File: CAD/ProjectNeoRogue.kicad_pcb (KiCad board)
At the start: 4 copper layers, 95.5 x 113.7 mm, 85 parts, among them J1 5v GND, J2 Micro_SD_Card, J3 JTAG, J4 UART, J5 Reset Jumper, J6 Boot Jumper, J7 RoundDisplay_SPI, J8 USB_C_Plug_USB2.0, J9 RoundDisplay_SPI_v2, SW1 SW_SPDT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

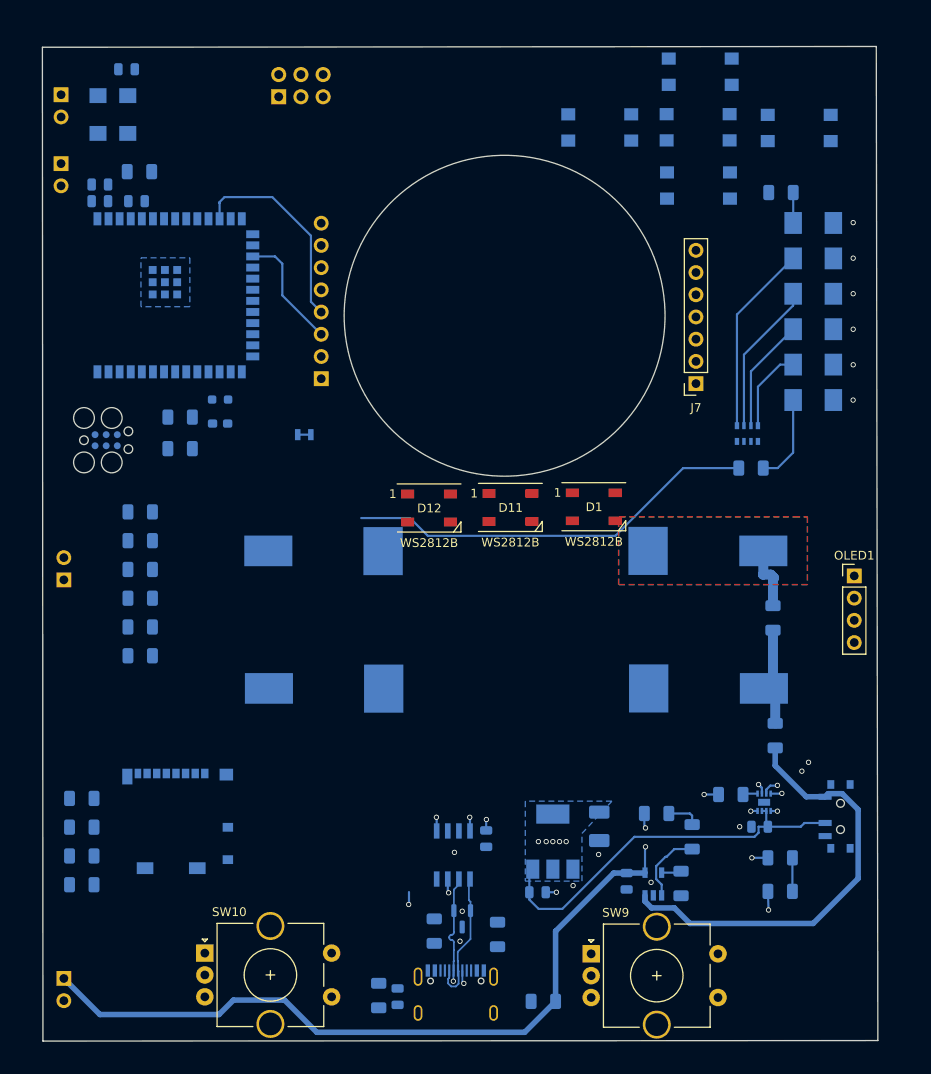
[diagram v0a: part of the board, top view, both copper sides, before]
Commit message: routing and removing buttons OLED
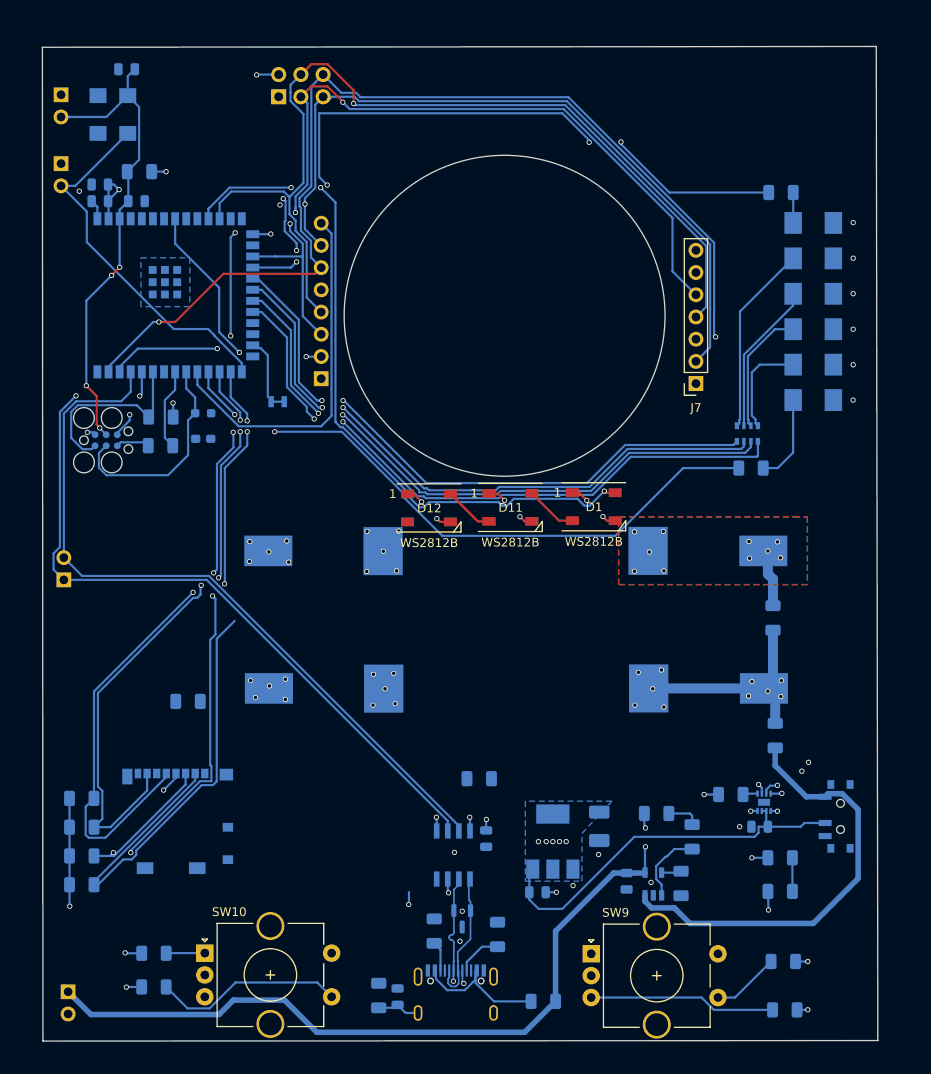
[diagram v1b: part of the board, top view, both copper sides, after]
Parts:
- removed OLED1: OLED, Connector_PinHeader_2.54mm:PinHeader_1x04_P2.54mm_Vertical
- removed SW4: SW_Up, BadgePirates:SW_SPST_TL3305C(small)
- removed SW5: SW_Center, BadgePirates:SW_SPST_TL3305C(small)
- removed SW6: SW_Right, BadgePirates:SW_SPST_TL3305C(small)
- removed SW7: SW_Down, BadgePirates:SW_SPST_TL3305C(small)
- removed SW8: SW_Left, BadgePirates:SW_SPST_TL3305C(small)
- moved R15 91.2 mm to (207.7, 155.9), turned to 0 degrees
- moved R16 86.1 mm to (207.5, 150.4), turned to 180 degrees
- moved R14 49.3 mm to (172.8, 129.5)
- moved R17 40.6 mm to (135.6, 149.5)
- moved R19 37.9 mm to (135.6, 153.3)
- moved R18 10.1 mm to (139.5, 120.7)
- moved JP1 4.84 mm to (150.0, 86.4)
- moved C11 2.60 mm to (141.2, 90.6)
- moved R21 2.49 mm to (141.2, 87.7)
- moved R24 2.27 mm to (136.3, 91.4)
- moved R22 2.20 mm to (136.4, 88.1)
- moved J1 1.60 mm to (125.8, 153.9)
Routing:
- net IO02: track 0.00 -> 120.4 mm, vias 0 -> 5
- net IO01: track 0.00 -> 119.7 mm, vias 0 -> 2
- net USB_TX_ESP_RX: track 0.00 -> 89.2 mm, vias 0 -> 2
- net USB_RX_ESP_TX: track 0.00 -> 85.9 mm
- net IO10: track 0.00 -> 83.2 mm, vias 0 -> 6
- net IO08: track 103.3 -> 185.5 mm, vias 2 -> 3
- net IO09: track 98.9 -> 179.8 mm, vias 2 -> 5
- net IO18: track 0.00 -> 80.6 mm, vias 0 -> 3
- net IO35: track 0.00 -> 80.0 mm, vias 0 -> 6
- net IO36: track 0.00 -> 74.7 mm, vias 0 -> 4
- net IO14: track 0.00 -> 73.9 mm, vias 0 -> 2
- net IO13: track 0.00 -> 72.9 mm, vias 0 -> 2
- net IO12: track 0.00 -> 72.4 mm, vias 0 -> 2
- net IO11: track 0.00 -> 71.3 mm, vias 0 -> 2
- net IO37: track 0.00 -> 70.4 mm, vias 0 -> 4
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
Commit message: Update ProjectNeoRogue.kicad_pcb
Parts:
- moved R18 32.3 mm to (135.5, 152.8)
- moved R19 25.7 mm to (160.1, 145.9), turned to 180 degrees
- moved R17 3.09 mm to (135.5, 146.4)
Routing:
- net IO05: track 21.3 -> 186.4 mm, vias 0 -> 6
- net IO04: track 0.00 -> 142.9 mm, vias 0 -> 9
- net IO17: track 0.00 -> 107.2 mm, vias 0 -> 4
- net IO16: track 4.43 -> 102.2 mm, vias 0 -> 4
- net IO19: track 21.8 -> 10.2 mm
- net VCC: track 50.9 -> 57.1 mm, vias 25 -> 26
- net GND: track 20.2 -> 18.6 mm, vias 45 -> 48
- net IO02: track 120.4 -> 119.3 mm
- net IO10: track 83.2 -> 82.4 mm
- net IO14: track 73.9 -> 74.6 mm
- net IO08: track 185.5 -> 184.9 mm

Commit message: updates
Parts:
- added J10: Conn_01x01_Socket, Connector_PinHeader_2.54mm:PinHeader_1x01_P2.54mm_Vertical, B.Cu at (134.0, 98.0)
- J2: footprint Connector_Card:microSD_HC_Molex_104031-0811 -> BadgePirates:TF_PUSH
- moved R12 20.6 mm to (128.9, 117.8)
- moved R13 20.6 mm to (128.9, 121.1)
- moved R5 20.6 mm to (128.9, 111.2)
- moved R6 20.6 mm to (128.9, 114.5)
- moved J2 0.75 mm to (138.8, 133.9), turned to 90 degrees
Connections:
- J2 pad 10: (no net) -> GND
- J2 pad 2: IO34 -> unconnected-(J2-DAT3/CD-Pad2)
- J2 pad 3: IO35 -> IO34
- J2 pad 4: VCC -> IO35
- J2 pad 5: IO36 -> VCC
- J2 pad 6: GND -> IO36
- J2 pad 7: IO37 -> GND
- J2 pad 8: unconnected-(J2-DAT1-Pad8) -> IO37
- J2 pad 9: GND -> unconnected-(J2-DET-Pad9)
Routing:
- net IO34: track 55.9 -> 0.81 mm
- net IO35: track 80.0 -> 43.9 mm, vias 6 -> 4
- net IO36: track 74.7 -> 40.3 mm
- net IO37: track 70.4 -> 41.5 mm
- net IO04: track 142.9 -> 131.6 mm, vias 9 -> 7
- net VCC: track 57.1 -> 54.6 mm, vias 26 -> 25
- net GND: track 18.6 -> 20.5 mm, vias 48 -> 50
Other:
- board text removed: "MicroSD"

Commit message: routing and cleanup
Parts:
- moved J1 5.60 mm to (127.3, 148.5)
- moved R6 3.33 mm to (128.9, 111.2)
- moved R5 3.14 mm to (128.9, 114.4)
- moved J4 2.81 mm to (127.9, 105.9)
- moved J10 1.02 mm to (134.0, 97.0)
- moved J8 0.60 mm to (170.1, 152.7)
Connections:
- net SCL renamed IO07
- net SDA renamed IO06
- U2 pad 13: unconnected-(U2-GPIO19/U1RTS/ADC2_CH8/CLK_OUT2/USB_D--Pad13) -> IO19
- U2 pad 16: IO46 -> unconnected-(U2-GPIO46-Pad16)
- U2 pad 23: IO21 -> unconnected-(U2-GPIO21-Pad23)
- U2 pad 24: IO47 -> unconnected-(U2-GPIO47/SPICLK_P/SUBSPICLK_P_DIFF-Pad24)
- U2 pad 26: IO45 -> unconnected-(U2-GPIO45-Pad26)
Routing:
- net IO19: track 10.2 -> 98.2 mm, vias 0 -> 4
- net IO34: track 0.81 -> 48.0 mm, vias 0 -> 6
- net IO37: track 41.5 -> 73.9 mm
- net IO36: track 40.3 -> 71.7 mm
- net IO35: track 43.9 -> 69.2 mm
- net IO05: track 186.4 -> 167.2 mm, vias 6 -> 10
- net TDI: track 0.00 -> 16.2 mm, vias 0 -> 2
- net /Power/BATTERY2+: track 26.9 -> 13.7 mm
- net IO04: track 131.6 -> 142.8 mm
- net Boot: track 42.2 -> 48.0 mm
- net IO01: track 119.7 -> 124.3 mm
- net IO15: track 90.5 -> 94.3 mm
- net IO02: track 119.3 -> 123.1 mm
- net Net-(C11-Pad1): track 0.00 -> 2.94 mm
- net RESET: track 54.9 -> 57.6 mm
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- added copper zone on B.Cu, net /Power/BATTERY2+
- removed copper zone on F.Cu, net /Power/BATTERY1+

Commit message: Updated pins and moar
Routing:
- net Boot: track 48.0 -> 47.4 mm
- net GND: vias 52 -> 44
- net /Power/BATTERY2+: vias 10 -> 0
- net /Power/BATTERY1+: vias 10 -> 0

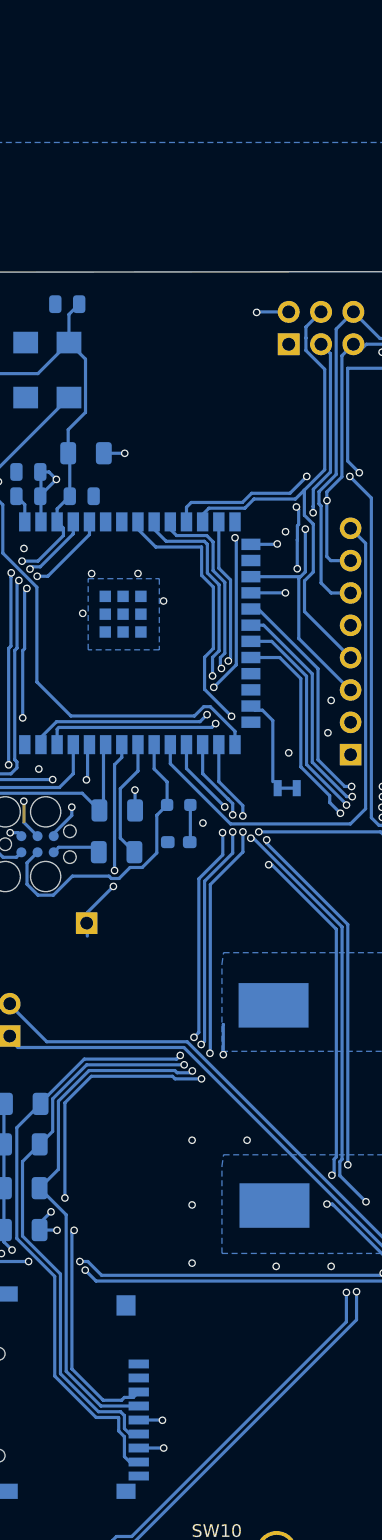
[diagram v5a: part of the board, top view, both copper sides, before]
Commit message: Updated layout
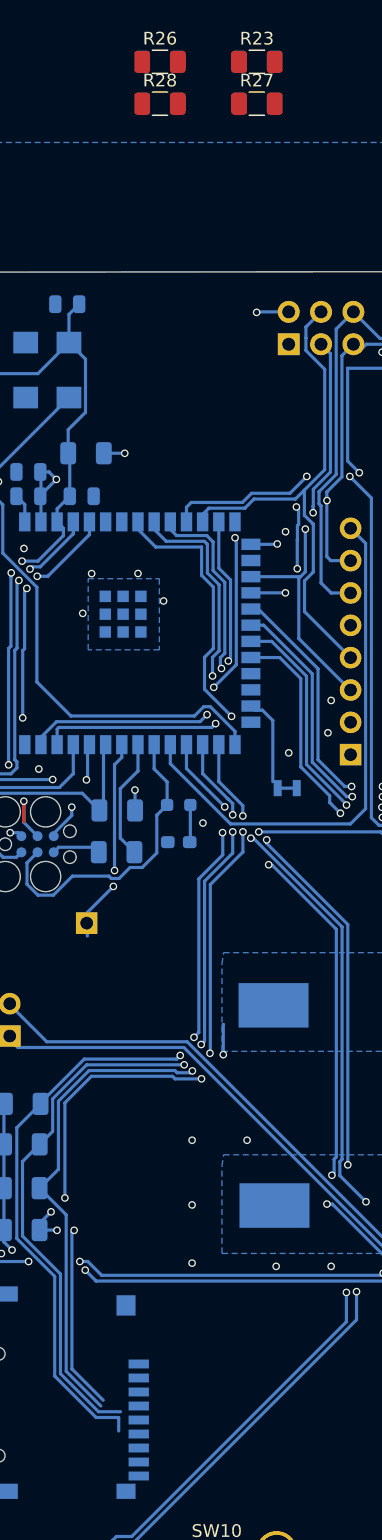
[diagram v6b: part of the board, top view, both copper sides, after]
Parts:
- added R23: 4.7k, BadgePirates:R_1206_3216Metric, F.Cu at (147.3, 29.3)
- added R26: 4.7k, BadgePirates:R_1206_3216Metric, F.Cu at (139.7, 29.3)
- added R27: 4.7k, BadgePirates:R_1206_3216Metric, F.Cu at (147.3, 32.6)
- added R28: 4.7k, BadgePirates:R_1206_3216Metric, F.Cu at (139.7, 32.6)
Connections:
- J2 pad 2: unconnected-(J2-DAT3/CD-Pad2) -> IO47
- J2 pad 3: IO34 -> IO35
- J2 pad 4: IO35 -> VCC
- J2 pad 5: VCC -> IO36
- J2 pad 6: IO36 -> GND
- J2 pad 7: GND -> IO37
- J2 pad 8: IO37 -> unconnected-(J2-DAT1-Pad8)
- R13 pad 1: IO34 -> IO47
- R16 pad 2: IO25 -> IO20
- SW9 pad S1: IO25 -> IO20
- U2 pad 14: unconnected-(U2-GPIO20/U1CTS/ADC2_CH9/CLK_OUT1/USB_D+-Pad14) -> IO20
- U2 pad 15: IO03 -> unconnected-(U2-GPIO3/TOUCH3/ADC1_CH2-Pad15)
- U2 pad 24: unconnected-(U2-GPIO47/SPICLK_P/SUBSPICLK_P_DIFF-Pad24) -> IO47
- U5 pad 7: IO09 -> IO07
- U5 pad 8: IO08 -> IO06
- X1 pad 3: IO08 -> IO06
- X1 pad 4: IO09 -> IO07
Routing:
- net IO34: track 48.0 -> 0.00 mm, vias 6 -> 0
- net IO47: track 0.00 -> 45.0 mm, vias 0 -> 6
- net IO25: track 7.78 -> 0.00 mm
- net IO20: track 0.00 -> 7.78 mm
- net IO37: track 73.9 -> 70.4 mm
- net IO35: track 69.2 -> 66.3 mm
- net IO36: track 71.7 -> 69.0 mm
- net unconnected-(U2-GPIO3/TOUCH3/ADC1_CH2-Pad15): track 0.00 -> 2.08 mm, vias 0 -> 1
- net IO03: track 2.08 -> 0.00 mm, vias 1 -> 0
- net GND: track 20.5 -> 18.6 mm, vias 44 -> 43
- net VCC: track 54.1 -> 52.3 mm, vias 25 -> 24

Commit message: Routing progress
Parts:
- added JP2: GPIO1, BadgePirates:SMT-JUMPER_2_NC_TRACE_NO-SILK, F.Cu at (-4.23, -0.13)
- added JP3: GPIO1, BadgePirates:SMT-JUMPER_2_NC_TRACE_NO-SILK, F.Cu at (-4.23, 2.14)
- added R29: 10k, BadgePirates:R_1206_3216Metric, F.Cu at (-8.36, 0.38)
- added R30: 10k, BadgePirates:R_1206_3216Metric, F.Cu at (-8.36, 3.67)
- D9: value Pwr -> PWR
- R21: value 75 -> 75k
- R23, R26, R27, R28: moved to B.Cu
- R24: value 22 -> 22k
- SW1: value SW_SPDT -> On/Off
- moved R26 121.8 mm to (214.9, 125.2), turned to -90 degrees
- moved R28 117.5 mm to (212.1, 125.2), turned to 90 degrees
- moved R23 70.7 mm to (202.4, 73.7), turned to 180 degrees
- moved R27 66.4 mm to (202.4, 69.6), turned to 180 degrees
- moved R4 0.12 mm to (133.9, 60.2)
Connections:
- J9 pad 5: IO33 -> IO21
- U2 pad 16: unconnected-(U2-GPIO46-Pad16) -> IO46
- U2 pad 23: unconnected-(U2-GPIO21-Pad23) -> IO21
- U2 pad 26: unconnected-(U2-GPIO45-Pad26) -> IO45
- X1 pad 5: IO01 -> Net-(JP2-B)
- X1 pad 6: IO02 -> Net-(JP3-A)
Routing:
- net IO20: track 7.78 -> 135.5 mm, vias 0 -> 4
- net IO09: track 178.4 -> 57.0 mm, vias 5 -> 2
- net IO08: track 184.7 -> 102.0 mm, vias 3 -> 4
- net IO10: track 80.3 -> 40.3 mm
- net IO47: track 45.0 -> 79.8 mm, vias 6 -> 8
- net IO02: track 123.1 -> 98.3 mm, vias 5 -> 7
- net GND: track 18.6 -> 23.0 mm, vias 43 -> 114
- net IO01: track 124.3 -> 128.2 mm, vias 2 -> 1
- net IO35: track 66.3 -> 68.8 mm
- net IO36: track 69.0 -> 70.7 mm
- net IO06: track 0.00 -> 1.68 mm
- net VCC: track 52.3 -> 53.9 mm, vias 24 -> 26
- net IO37: track 70.4 -> 71.9 mm

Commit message: Layout ready for cleanup
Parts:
- JP2, JP3, R29, R30: moved to B.Cu
- moved R29 179.6 mm to (164.1, 50.5), turned to -90 degrees
- moved R30 175.7 mm to (158.8, 57.9), turned to -90 degrees
- moved JP2 172.9 mm to (161.5, 49.0), turned to 180 degrees
- moved JP3 169.2 mm to (156.2, 55.9), turned to -90 degrees
- moved R28 3.30 mm to (215.4, 125.2)
- moved R26 2.03 mm to (212.9, 125.2)
- moved F1 1.16 mm to (206.6, 125.7)
- moved JP1 0.67 mm to (150.6, 86.4)
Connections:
- JP1 pad 2: IO48 -> (no net)
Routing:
- net IO06: track 1.68 -> 182.8 mm, vias 0 -> 3
- net IO07: track 0.00 -> 176.9 mm, vias 0 -> 3
- net IO45: track 0.00 -> 50.4 mm, vias 0 -> 2
- net IO10: track 40.3 -> 71.9 mm
- net IO09: track 57.0 -> 87.2 mm, vias 2 -> 1
- net IO46: track 0.00 -> 21.2 mm, vias 0 -> 2
- net IO01: track 128.2 -> 107.7 mm, vias 1 -> 4
- net IO02: track 98.3 -> 110.6 mm, vias 7 -> 4
- net IO21: track 0.00 -> 9.75 mm, vias 0 -> 1
- net Net-(SW1-A): track 50.0 -> 58.6 mm
- net Net-(JP2-B): track 0.00 -> 6.14 mm
- net VCC: track 53.9 -> 58.4 mm, vias 26 -> 28
- net IO08: track 102.0 -> 98.0 mm, vias 4 -> 2
- net Net-(JP3-A): track 0.00 -> 3.94 mm
- net unconnected-(U2-GPIO3/TOUCH3/ADC1_CH2-Pad15): track 2.08 -> 0.00 mm, vias 1 -> 0
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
